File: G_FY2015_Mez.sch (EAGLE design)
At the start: 197 parts, among them IC100 FT232RL, J1 RPI2_GPIO_HOLES, J100 EPL.00.250.NTN, J101 EPL.00.250.NTN, J102 EPL.00.250.NTN, J103 EPL.00.250.NTN, J180 TOKUDEN_SP6, J181 USB Mini-B Connector, J2 SPACEWIRE_MDMMDM9, J300 SHV_PIGTAIL_LAND, J301 SHV_PIGTAIL_LAND, J600_12V IL-4P-S3EN2, J610 2.1MMJACKTHM, U10 LM60, U100 AD9215, U101 AD8138, U102 LM6142, U11 MCP4822-E/SN, U110 AD9215, U111 AD8138, U112 LM6142, U120 AD9215, U121 AD8138, U122 LM6142, U130 AD9215, U131 AD8138, U132 LM6142, U190 SN65LVDS049, U191 GPS_FGPMMOPA6H, U192 LED-5, U300 OPTON_1PA_12, U301 OPTON_1PA_12, U302 2SC1815, U303 2SJ313, U5 MCP3208-CI/SL, U500 LT6106, U510 LT6106, U6 MCP1525TSOT-23-3, U600 PHT12050WAH, U610 PHT12050WAH, U620 LTC1983ES6-3, U7 LM60, U8 LM60, U9 LM60

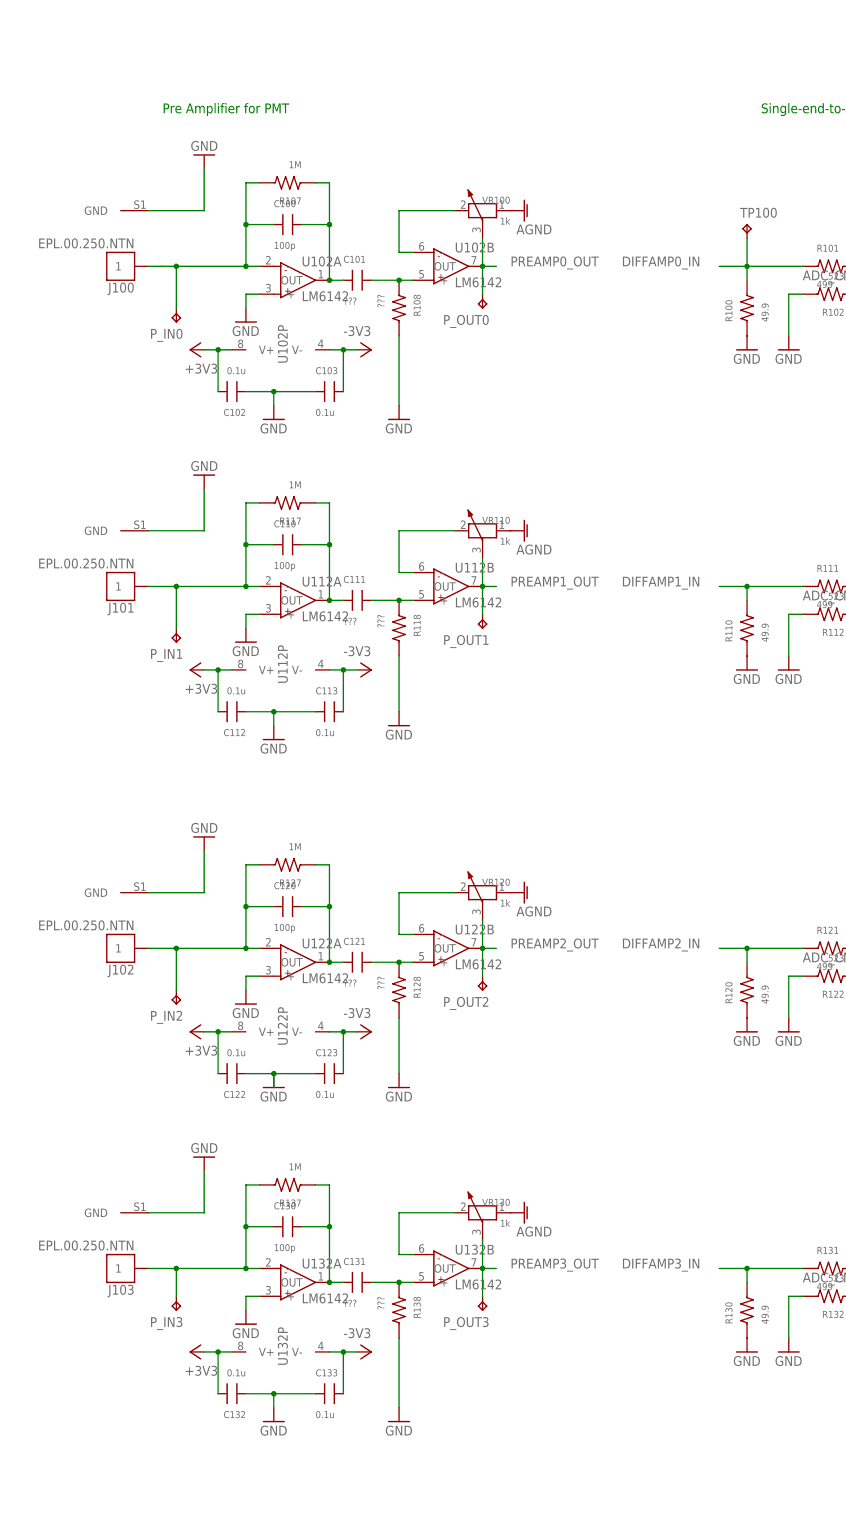
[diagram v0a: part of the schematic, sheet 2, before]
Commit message: +5V_BEFORE_SENSE and +3V3_BEFORE_SENSE properly connected (previously they were not connected)
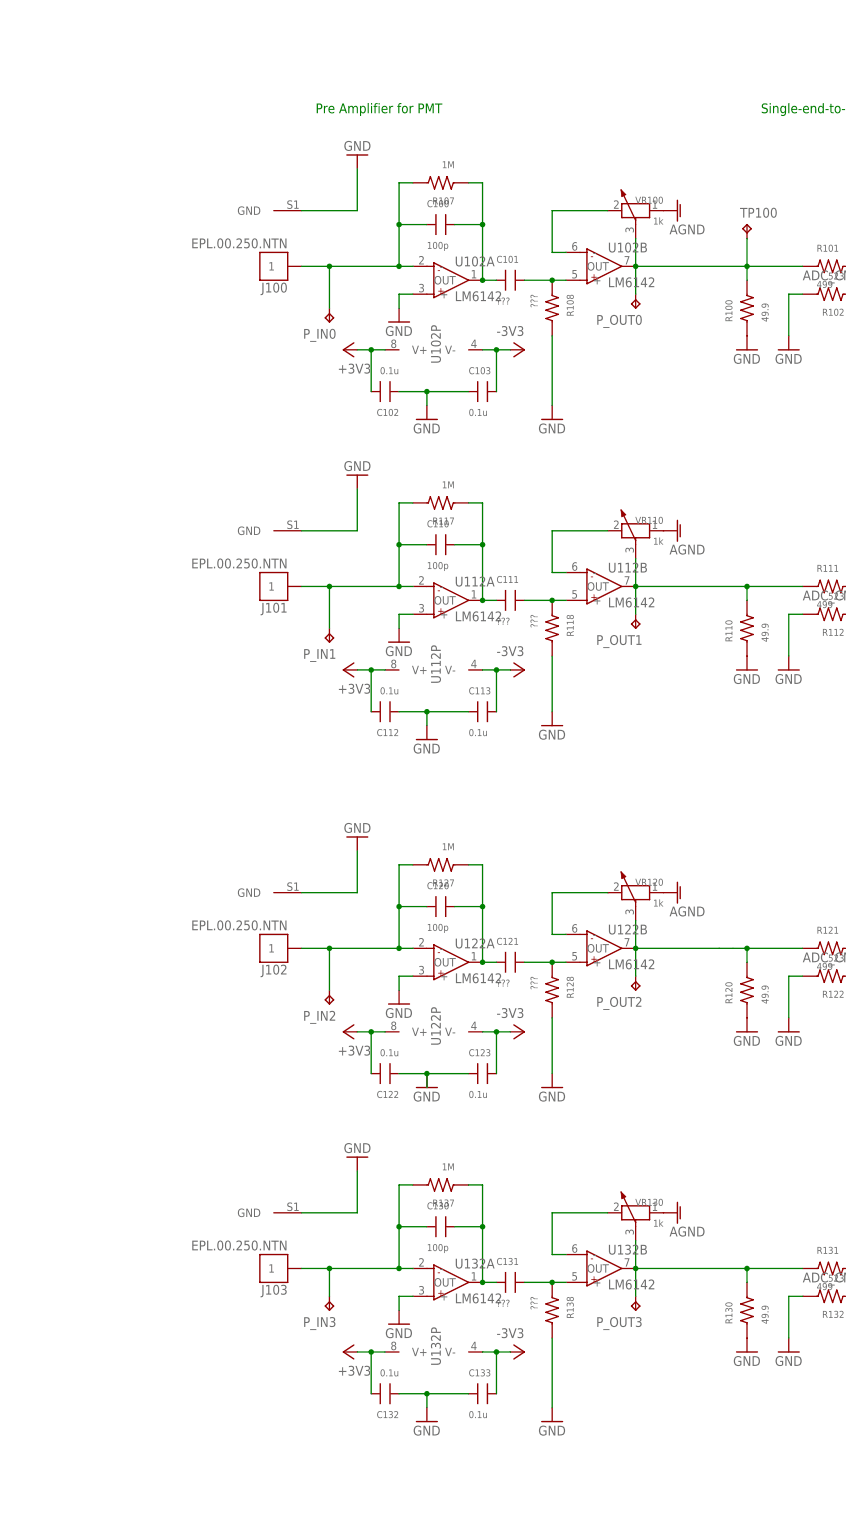
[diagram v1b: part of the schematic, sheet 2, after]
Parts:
- R302: value 100 -> 4.7k
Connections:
- removed net 3V3_BEFORE_SENSE: U610.V_O
- removed net 5V_BEFORE_SENSE: U600.V_O
- removed net DIFFAMP0_IN: R100.2, R101.1, TP100.TP
- removed net DIFFAMP1_IN: R110.2, R111.1
- removed net DIFFAMP2_IN: R120.2, R121.1
- removed net DIFFAMP3_IN: R130.2, R131.1
- net +3V3_BEFORE_SENSE: now also U610.V_O
- net +5V_BEFORE_SENSE: now also U600.V_O
- net PREAMP0_OUT: now also R100.2, R101.1, TP100.TP
- net PREAMP1_OUT: now also R110.2, R111.1
- net PREAMP2_OUT: now also R120.2, R121.1
- net PREAMP3_OUT: now also R130.2, R131.1
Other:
- moved on the sheet: C100, C101, C102, C103, C110, C111, C112, C113, C120, C121, C122, C123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
